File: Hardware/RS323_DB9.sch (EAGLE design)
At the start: 16 parts, among them U2 XN04312

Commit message: Fixed headers, trace re route
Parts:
- JP2: device SparkFun-Connectors:M04LOCK -> SparkFun-Connectors:M04PTH
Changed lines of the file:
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@@
 <part name="P+5" library="SparkFun" deviceset="VCC" device=""/>
 <part name="GND1" library="SparkFun" deviceset="GND" device=""/>
-<part name="JP2" library="SparkFun-Connectors" deviceset="M04" device="LOCK"/>
+<part name="JP2" library="SparkFun-Connectors" deviceset="M04" device="PTH"/>
 <part name="E$1" library="SparkFun" deviceset="FIDUCIAL" device="1X2"/>
 <part name="E$2" library="SparkFun" deviceset="FIDUCIAL" device="1X2"/>

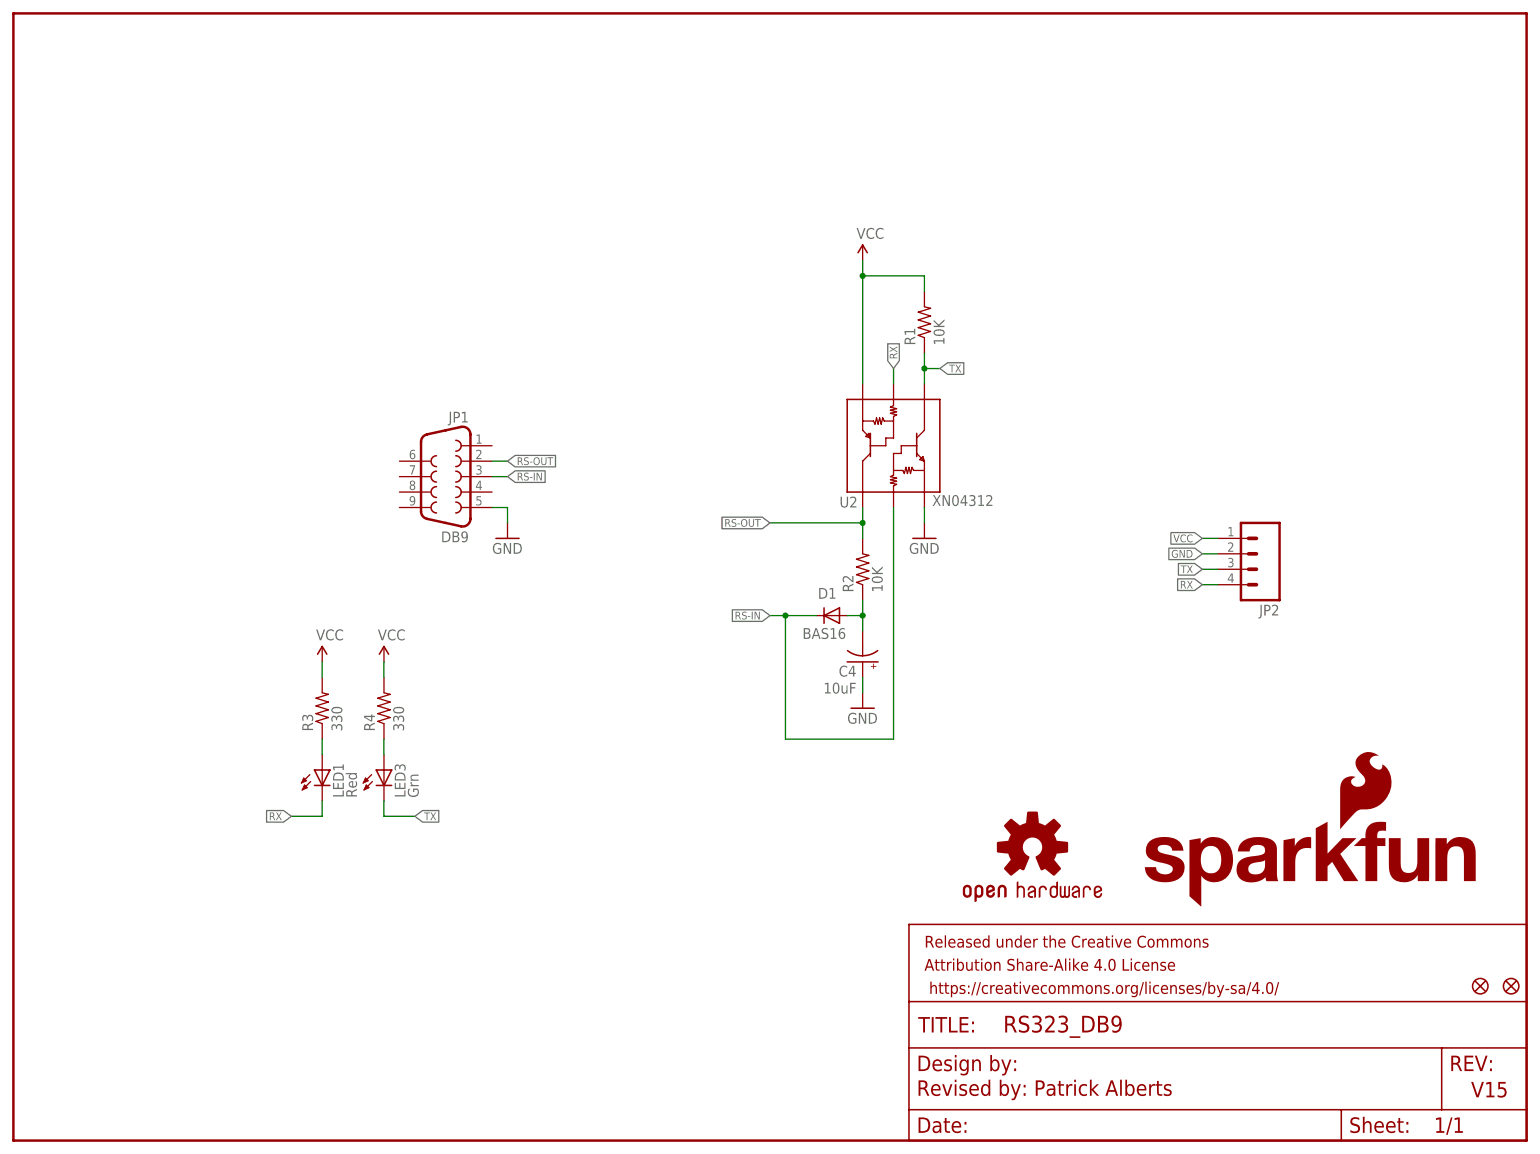
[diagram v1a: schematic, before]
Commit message: fixed bad trace, added top ground plane.
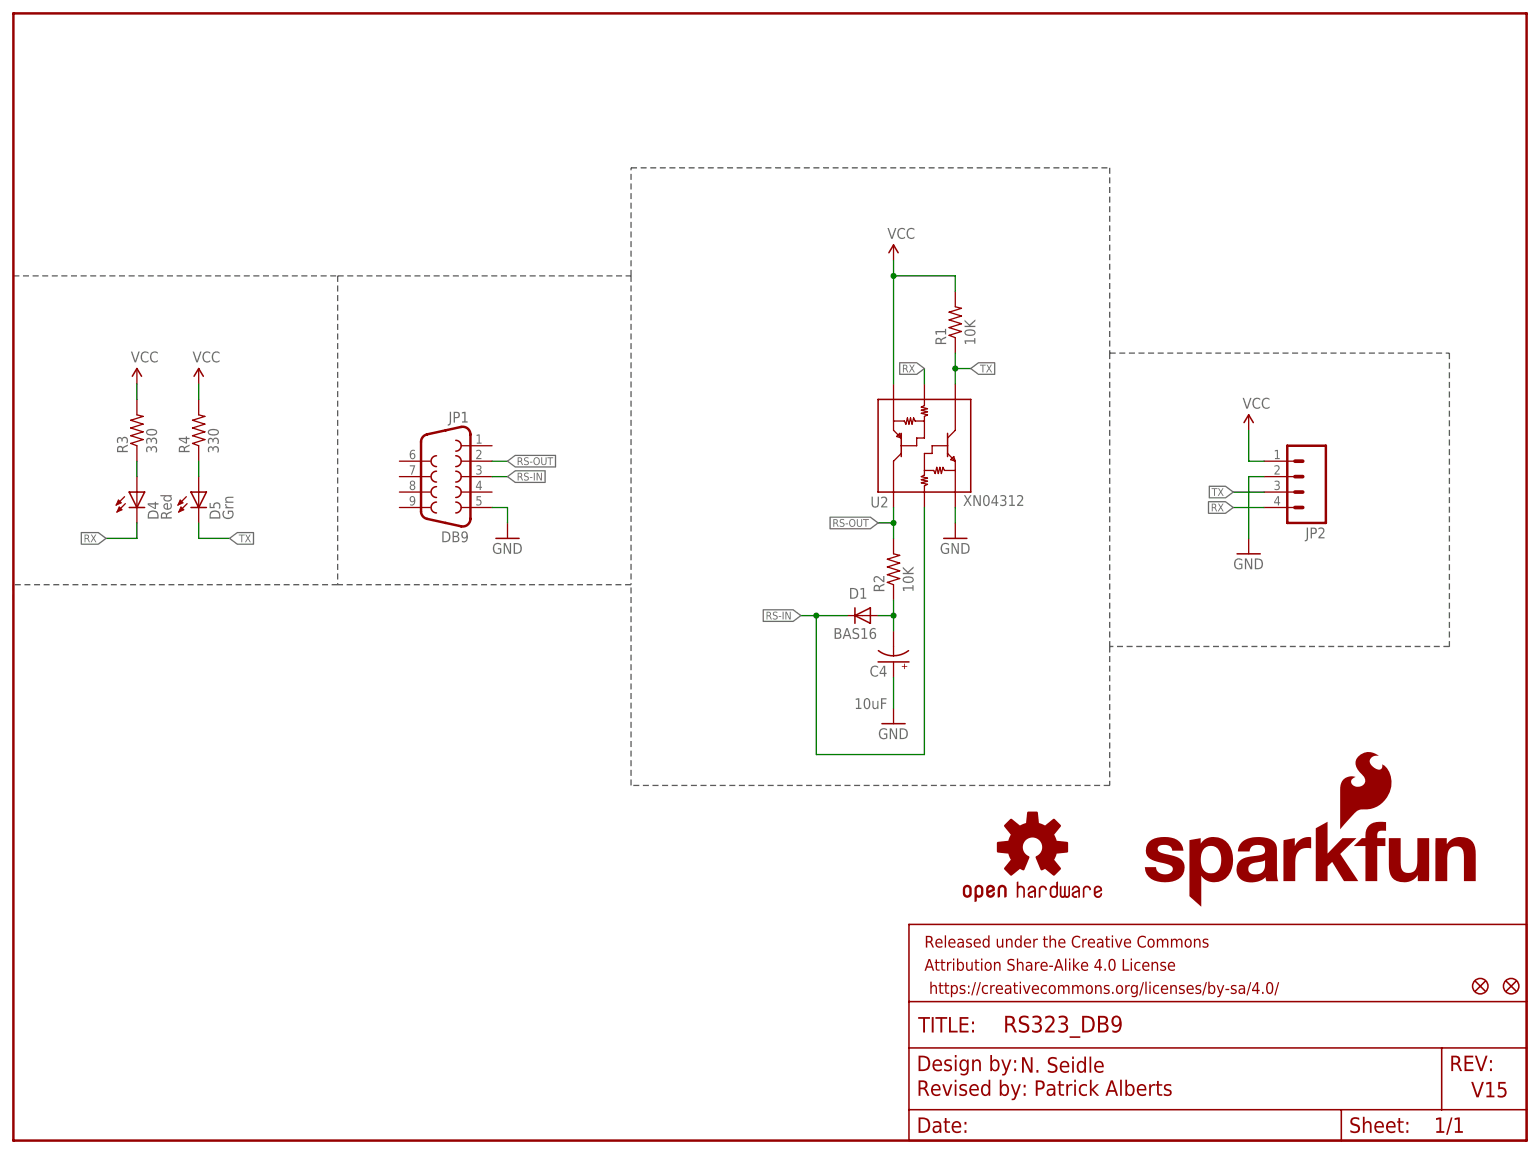
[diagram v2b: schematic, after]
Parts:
- removed LED1: Red, SparkFun:LED1206
- removed LED3: Grn, SparkFun:LED1206
- added D4: Red, SparkFun:LED1206
- added D5: Grn, SparkFun:LED1206
- FRAME1: value FRAME-LETTER -> (none)
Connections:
- net N$1: now also D4.A; no longer LED1.A
- net N$2: now also D5.A; no longer LED3.A
- net RX: now also D4.C; no longer LED1.C
- net TX: now also D5.C; no longer LED3.C
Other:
- note added: "N. Seidle"
- moved on the sheet: C4, D1, JP2, R1, R2, R3, R4, U2
